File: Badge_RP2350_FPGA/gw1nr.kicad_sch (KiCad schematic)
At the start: 16 parts, among them U2 GW1N-LV9QN88C6_I5_, U6 W25Q32JVSS

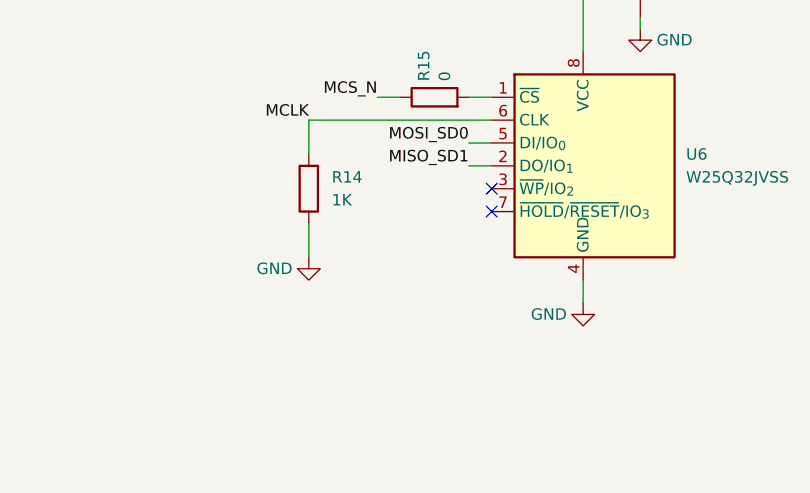
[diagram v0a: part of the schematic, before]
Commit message: Version 1.6: fix FB3 error, fix missing secondary flash pull-up, fix missing diode on battery, realign and add silkscreen
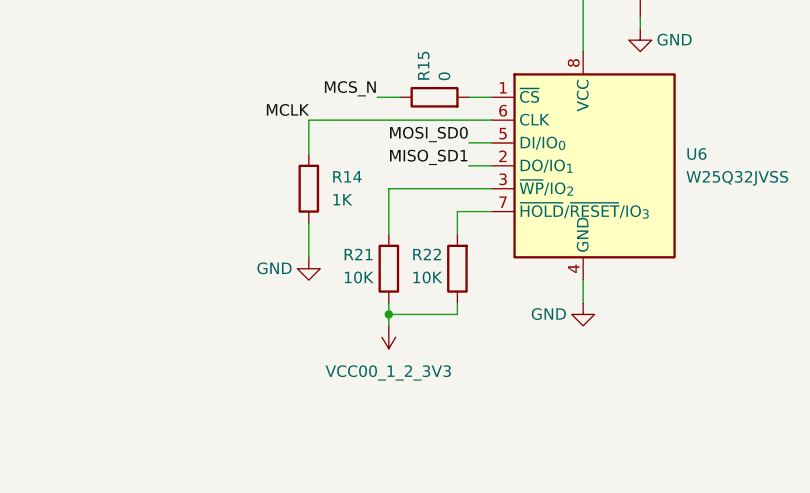
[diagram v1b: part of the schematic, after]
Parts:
- added R21, R22: 10K, Resistor_SMD:R_0402_1005Metric, symbol Device:R
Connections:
- net VCC00_1_2_3V3: now also R21.1, R22.1
- net at U6.3 (~{WP}/IO_{2}): now also R21.2
- net at U6.7 (~{HOLD}/~{RESET}/IO_{3}): now also R22.2
- no-connect marks 47 -> 45

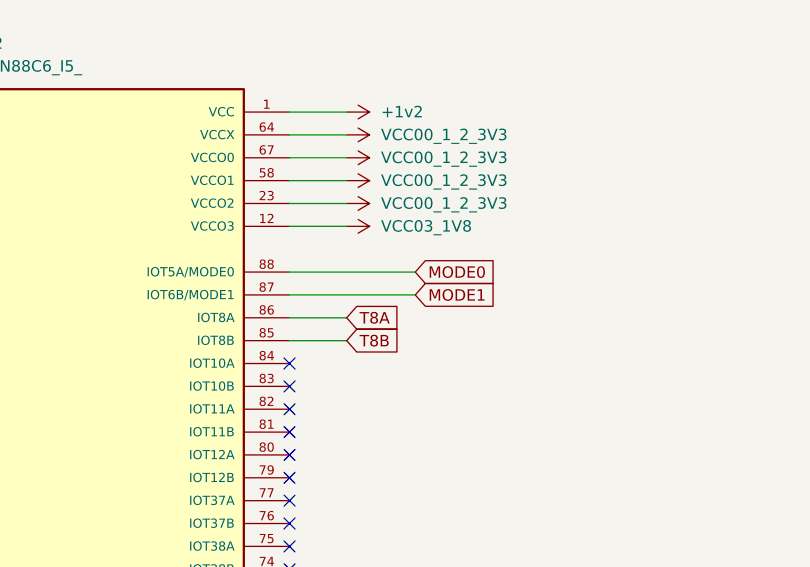
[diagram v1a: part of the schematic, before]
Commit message: fix power boost issue
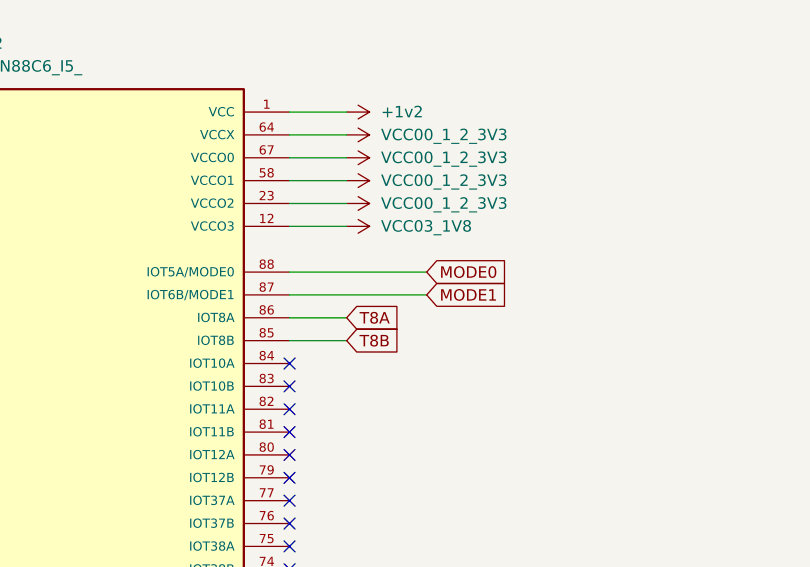
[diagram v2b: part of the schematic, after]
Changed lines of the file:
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@@
 	(wire
 		(pts
-			(xy 138.43 59.69) (xy 152.4 59.69)
+			(xy 138.43 59.69) (xy 153.67 59.69)
 		)
 		(stroke
@@
 	(wire
 		(pts
-			(xy 138.43 62.23) (xy 152.4 62.23)
+			(xy 138.43 62.23) (xy 153.67 62.23)
 		)
 		(stroke
@@
 	(global_label "MODE1"
 		(shape input)
-		(at 152.4 62.23 0)
+		(at 153.67 62.23 0)
 		(fields_autoplaced yes)
 		(effects
@@
 		)
 		(property "Intersheetrefs" "${INTERSHEET_REFS}"
-			(at 161.7956 62.23 0)
+			(at 163.0656 62.23 0)
 			(hide yes)
 			(show_name no)
@@
 	(global_label "MODE0"
 		(shape input)
-		(at 152.4 59.69 0)
+		(at 153.67 59.69 0)
 		(fields_autoplaced yes)
 		(effects
@@
 		)
 		(property "Intersheetrefs" "${INTERSHEET_REFS}"
-			(at 161.7956 59.69 0)
+			(at 163.0656 59.69 0)
 			(hide yes)
 			(show_name no)

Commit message: put pull up to mode1, pull down to mode0
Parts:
- added R23: 1K, Resistor_SMD:R_0402_1005Metric, symbol Device:R
- added R24: 4.7K, Resistor_SMD:R_0402_1005Metric, symbol Device:R
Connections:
- net GND: now also R23.2
- net MODE0: now also R23.1
- net MODE1: now also R24.2
- net VCC03_1V8: now also R24.1
- net T8A: no longer names the net of U2.86 (IOT8A)
- net T8B: no longer names the net of U2.85 (IOT8B)
- no-connect marks 45 -> 47
